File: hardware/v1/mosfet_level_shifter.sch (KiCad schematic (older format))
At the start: 3 parts, among them Q1 2N7000

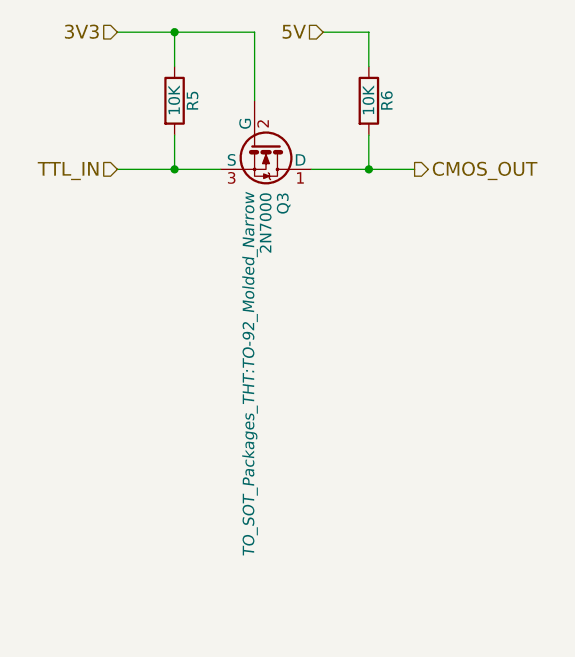
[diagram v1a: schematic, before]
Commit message: Complete piconnect circuit and start routing.
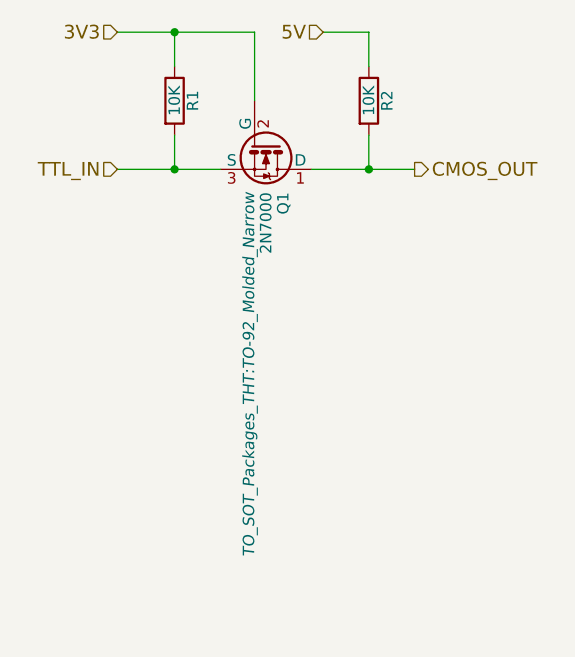
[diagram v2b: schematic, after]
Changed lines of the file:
@@
 AR Path="/57A33FC0/5798C5FD" Ref="R3"  Part="1"
 AR Path="/57A33FD2/5798C5FD" Ref="R5"  Part="1"
-F 0 "R5" V 1230 1000 50  0000 C CNN
+F 0 "R1" V 1230 1000 50  0000 C CNN
 F 1 "10K" V 1150 1000 50  0000 C CNN
 F 2 "Resistors_ThroughHole:Resistor_Horizontal_RM10mm" V 1080 1000 50  0001 C CNN
@@
 AR Path="/57A33FC0/5798C628" Ref="R4"  Part="1"
 AR Path="/57A33FD2/5798C628" Ref="R6"  Part="1"
-F 0 "R6" V 2080 1000 50  0000 C CNN
+F 0 "R2" V 2080 1000 50  0000 C CNN
 F 1 "10K" V 2000 1000 50  0000 C CNN
 F 2 "Resistors_ThroughHole:Resistor_Horizontal_RM10mm" V 1930 1000 50  0001 C CNN
@@
 AR Path="/57A33FC0/5798C66E" Ref="Q2"  Part="1"
 AR Path="/57A33FD2/5798C66E" Ref="Q3"  Part="1"
-F 0 "Q3" H 1750 1275 50  0000 L CNN
+F 0 "Q1" H 1750 1275 50  0000 L CNN
 F 1 "2N7000" H 1750 1200 50  0000 L CNN
 F 2 "TO_SOT_Packages_THT:TO-92_Molded_Narrow" H 1750 1125 50  0000 L CIN

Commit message: Add mosfet clock gates to I2C connector rows - because addresses conflict and the second bus (I2C0) cannot be used safely on the raspberry pi.
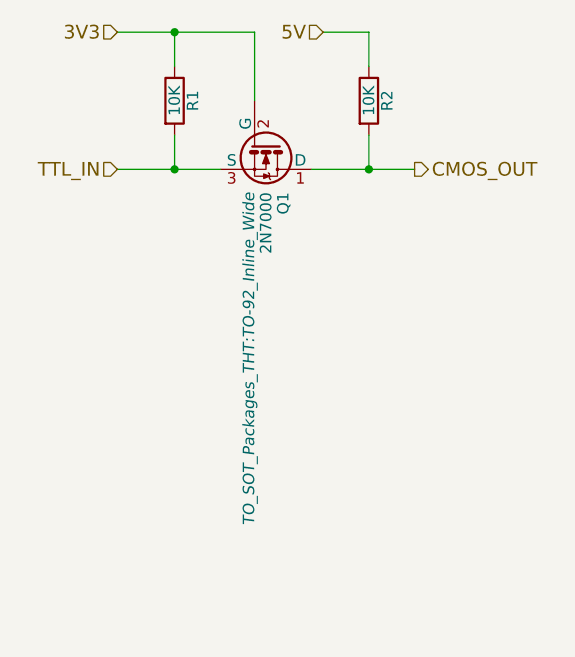
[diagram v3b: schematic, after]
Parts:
- Q1: footprint TO_SOT_Packages_THT:TO-92_Molded_Narrow -> TO_SOT_Packages_THT:TO-92_Inline_Wide
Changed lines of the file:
@@
 LIBS:contrib
 LIBS:valves
-LIBS:Pi2_Connector
-LIBS:MAX7221
-LIBS:MCP23S17
-LIBS:MCP23017
 LIBS:piconnect-cache
 EELAYER 25 0
@@
 $Descr A4 11693 8268
 encoding utf-8
-Sheet 7 6
+Sheet 2 6
 Title ""
 Date ""
@@
 F 0 "Q1" H 1750 1275 50  0000 L CNN
 F 1 "2N7000" H 1750 1200 50  0000 L CNN
-F 2 "TO_SOT_Packages_THT:TO-92_Molded_Narrow" H 1750 1125 50  0000 L CIN
+F 2 "TO_SOT_Packages_THT:TO-92_Inline_Wide" H 1750 1125 50  0000 L CIN
 F 3 "" H 1550 1200 50  0000 L CNN
 	1    1550 1200
